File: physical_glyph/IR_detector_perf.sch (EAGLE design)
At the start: 31 parts, among them IC1 7805T, T1 BP103, U1 MCP6004-I/P, U2 LM339PWR

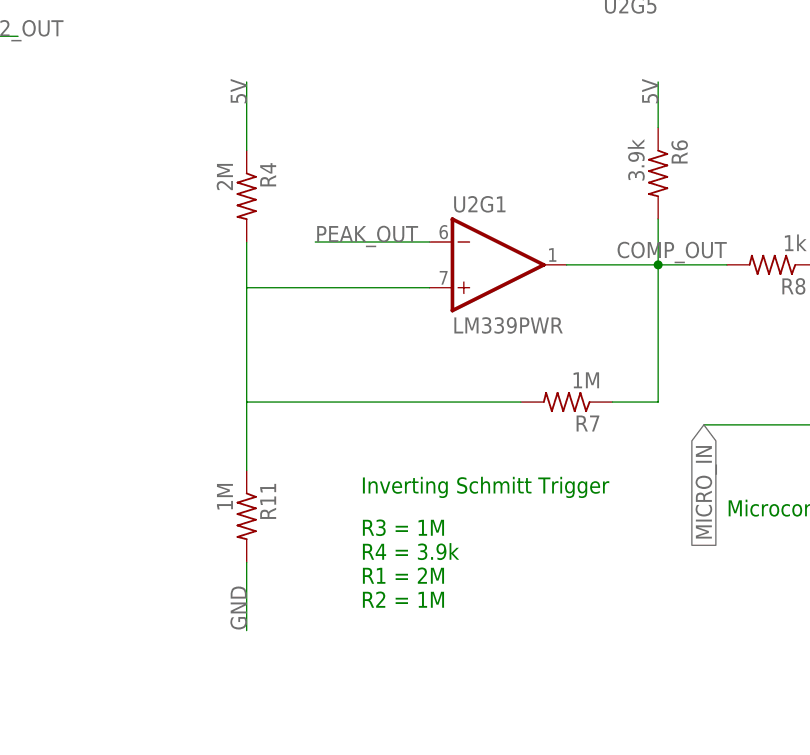
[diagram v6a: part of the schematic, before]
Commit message: Change hystersis upper limit to 2V
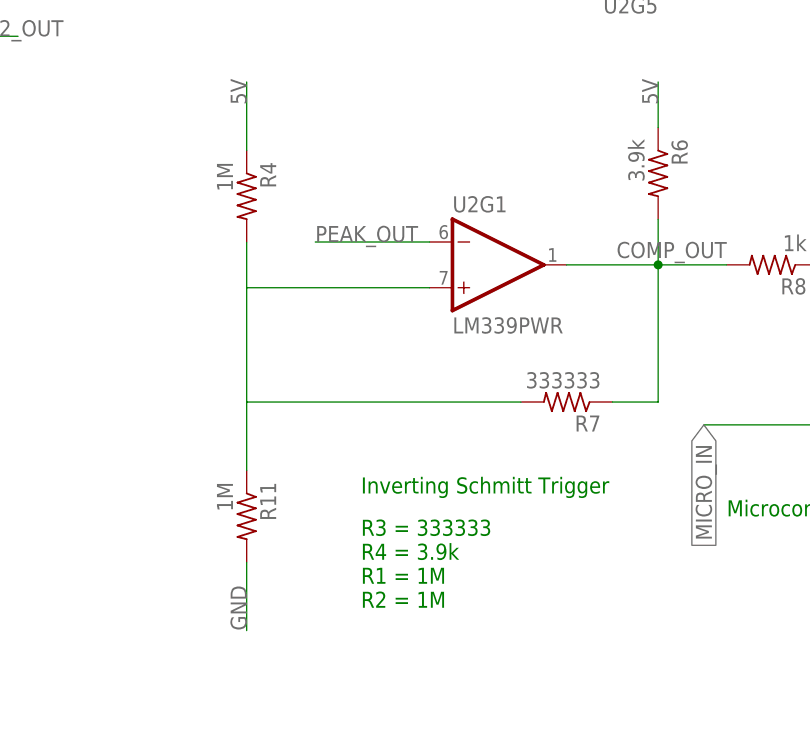
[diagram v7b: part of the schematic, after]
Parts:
- R4: value 2M -> 1M
- R7: value 1M -> 333333
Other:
- note added: "R3 = 333333 R4 = 3.9k R1 = 1M R2 = 1M"
- note removed: "R3 = 1M R4 = 3.9k R1 = 2M R2 = 1M"
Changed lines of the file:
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@@
 <part name="R2" library="rcl" library_urn="urn:adsk.eagle:library:334" deviceset="R-US_" device="0204/2V" package3d_urn="urn:adsk.eagle:package:23495/1" value="1k"/>
 <part name="R3" library="rcl" library_urn="urn:adsk.eagle:library:334" deviceset="R-US_" device="0204/2V" package3d_urn="urn:adsk.eagle:package:23495/1" value="10k"/>
-<part name="R4" library="rcl" library_urn="urn:adsk.eagle:library:334" deviceset="R-US_" device="0204/2V" package3d_urn="urn:adsk.eagle:package:23495/1" value="2M"/>
-<part name="R7" library="rcl" library_urn="urn:adsk.eagle:library:334" deviceset="R-US_" device="0204/2V" package3d_urn="urn:adsk.eagle:package:23495/1" value="1M"/>
+<part name="R4" library="rcl" library_urn="urn:adsk.eagle:library:334" deviceset="R-US_" device="0204/2V" package3d_urn="urn:adsk.eagle:package:23495/1" value="1M"/>
+<part name="R7" library="rcl" library_urn="urn:adsk.eagle:library:334" deviceset="R-US_" device="0204/2V" package3d_urn="urn:adsk.eagle:package:23495/1" value="333333"/>
 <part name="R11" library="rcl" library_urn="urn:adsk.eagle:library:334" deviceset="R-US_" device="0204/2V" package3d_urn="urn:adsk.eagle:package:23495/1" value="1M"/>
 <part name="C3" library="resistor" library_urn="urn:adsk.eagle:library:348" deviceset="C-EU" device="025-024X044" package3d_urn="urn:adsk.eagle:package:26149/1" value="0.1uF"/>
@@
 Amp B: Peak Detector
 Amp C: Split Rail Buffer</text>
-<text x="78.74" y="-27.94" size="1.778" layer="91">R3 = 1M
+<text x="78.74" y="-27.94" size="1.778" layer="91">R3 = 333333
 R4 = 3.9k
-R1 = 2M
+R1 = 1M
 R2 = 1M</text>
 <text x="12.7" y="-58.42" size="1.778" layer="91">RC value = peak detector "leak"</text>

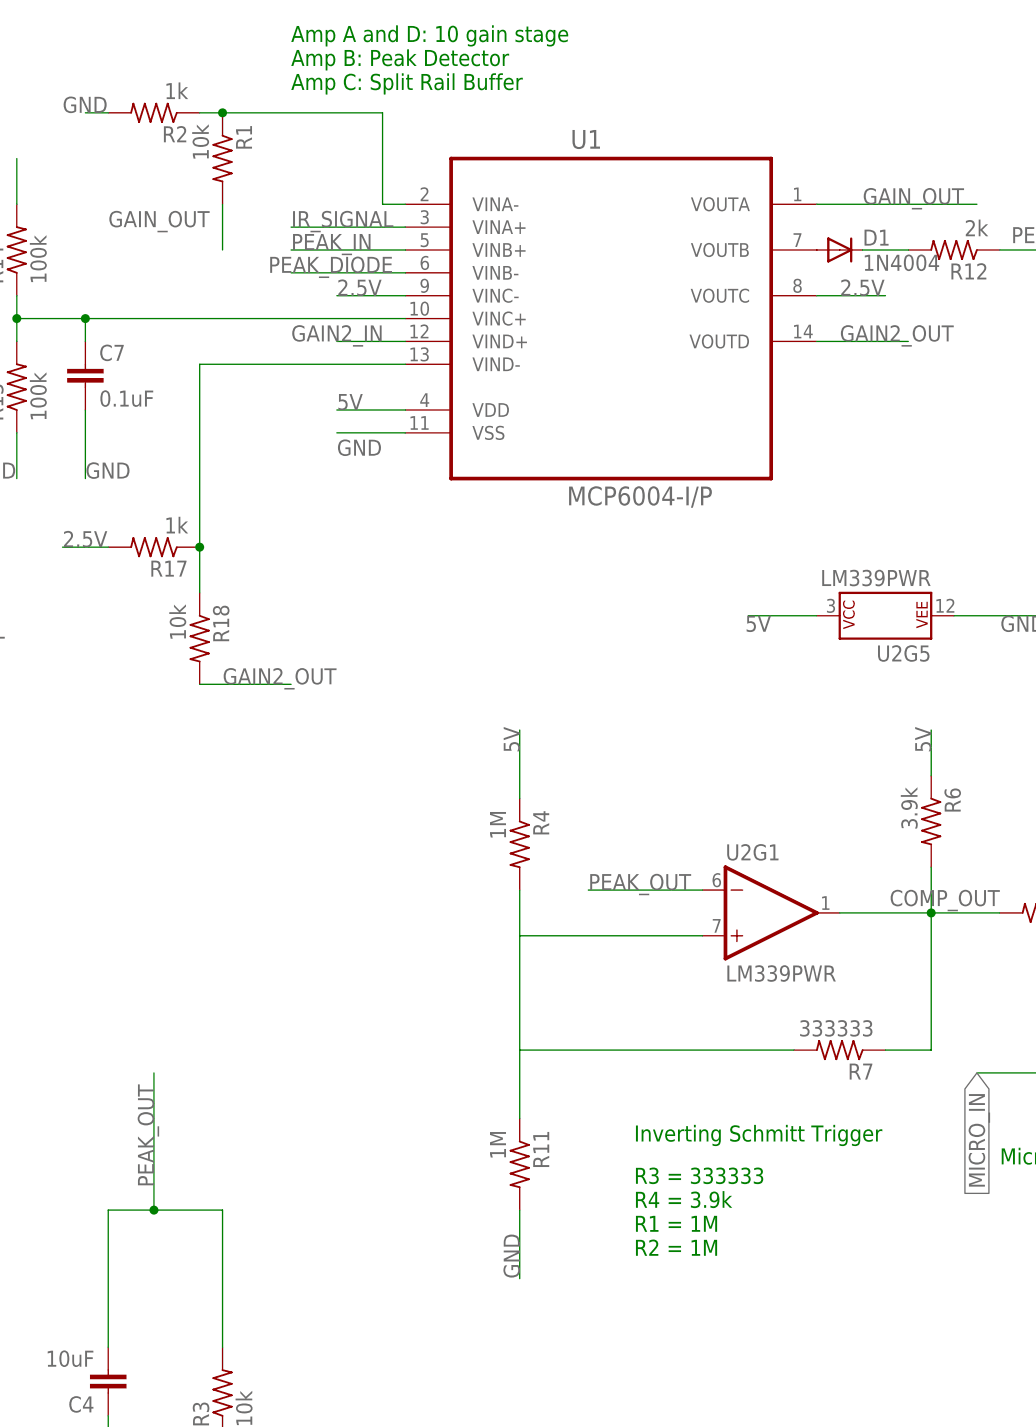
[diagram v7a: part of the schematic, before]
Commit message: Change gain resistors, fix net issue
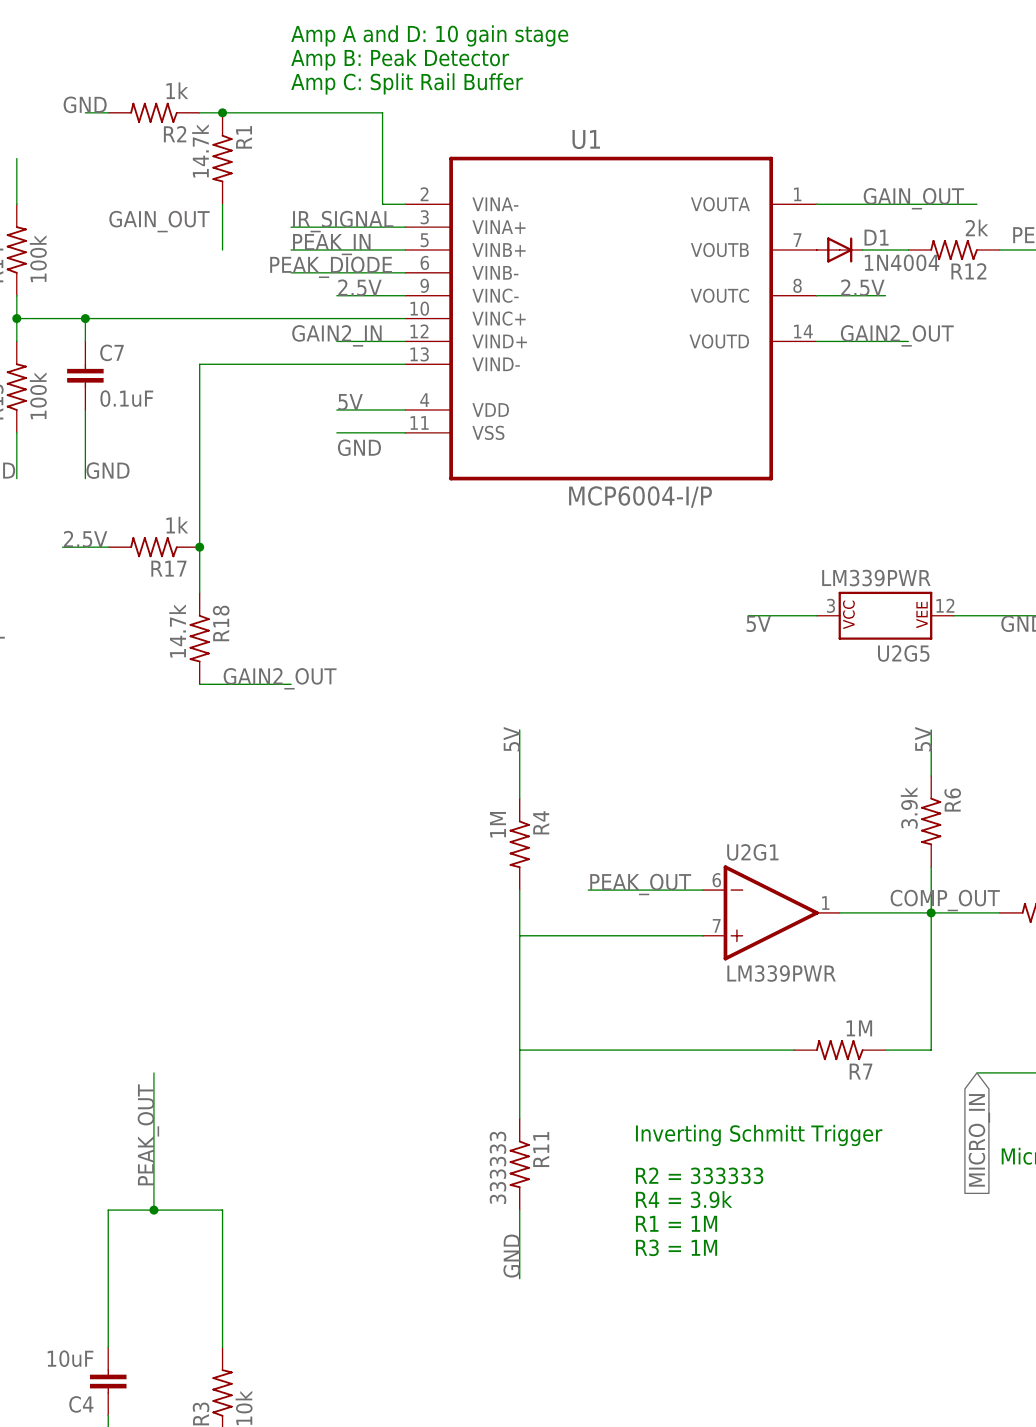
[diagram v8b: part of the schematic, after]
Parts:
- R1, R18: value 10k -> 14.7k
- R11: value 1M -> 333333
- R7: value 333333 -> 1M
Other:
- note added: "R2 = 333333 R4 = 3.9k R1 = 1M R3 = 1M"
- note removed: "R3 = 333333 R4 = 3.9k R1 = 1M R2 = 1M"
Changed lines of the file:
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@@
 <?xml version="1.0" encoding="utf-8"?>
 <!DOCTYPE eagle SYSTEM "eagle.dtd">
-<eagle version="8.6.0">
+<eagle version="9.0.0">
 <drawing>
 <settings>
@@
 <part name="R3" library="rcl" library_urn="urn:adsk.eagle:library:334" deviceset="R-US_" device="0204/2V" package3d_urn="urn:adsk.eagle:package:23495/1" value="10k"/>
 <part name="R4" library="rcl" library_urn="urn:adsk.eagle:library:334" deviceset="R-US_" device="0204/2V" package3d_urn="urn:adsk.eagle:package:23495/1" value="1M"/>
-<part name="R7" library="rcl" library_urn="urn:adsk.eagle:library:334" deviceset="R-US_" device="0204/2V" package3d_urn="urn:adsk.eagle:package:23495/1" value="333333"/>
-<part name="R11" library="rcl" library_urn="urn:adsk.eagle:library:334" deviceset="R-US_" device="0204/2V" package3d_urn="urn:adsk.eagle:package:23495/1" value="1M"/>
+<part name="R7" library="rcl" library_urn="urn:adsk.eagle:library:334" deviceset="R-US_" device="0204/2V" package3d_urn="urn:adsk.eagle:package:23495/1" value="1M"/>
+<part name="R11" library="rcl" library_urn="urn:adsk.eagle:library:334" deviceset="R-US_" device="0204/2V" package3d_urn="urn:adsk.eagle:package:23495/1" value="333333"/>
 <part name="C3" library="resistor" library_urn="urn:adsk.eagle:library:348" deviceset="C-EU" device="025-024X044" package3d_urn="urn:adsk.eagle:package:26149/1" value="0.1uF"/>
 <part name="C4" library="resistor" library_urn="urn:adsk.eagle:library:348" deviceset="C-EU" device="025-024X044" package3d_urn="urn:adsk.eagle:package:26149/1" value="10uF"/>
@@
 <part name="R15" library="rcl" library_urn="urn:adsk.eagle:library:334" deviceset="R-US_" device="0204/2V" package3d_urn="urn:adsk.eagle:package:23495/1" value="100k"/>
 <part name="C7" library="resistor" library_urn="urn:adsk.eagle:library:348" deviceset="C-EU" device="025-024X044" package3d_urn="urn:adsk.eagle:package:26149/1" value="0.1uF"/>
-<part name="R1" library="rcl" library_urn="urn:adsk.eagle:library:334" deviceset="R-US_" device="0204/2V" package3d_urn="urn:adsk.eagle:package:23495/1" value="10k"/>
+<part name="R1" library="rcl" library_urn="urn:adsk.eagle:library:334" deviceset="R-US_" device="0204/2V" package3d_urn="urn:adsk.eagle:package:23495/1" value="14.7k"/>
 <part name="C8" library="resistor" library_urn="urn:adsk.eagle:library:348" deviceset="C-EU" device="025-024X044" package3d_urn="urn:adsk.eagle:package:26149/1" value="0.1uF"/>
 <part name="R16" library="rcl" library_urn="urn:adsk.eagle:library:334" deviceset="R-US_" device="0204/2V" package3d_urn="urn:adsk.eagle:package:23495/1" value="100k"/>
 <part name="R17" library="rcl" library_urn="urn:adsk.eagle:library:334" deviceset="R-US_" device="0204/2V" package3d_urn="urn:adsk.eagle:package:23495/1" value="1k"/>
-<part name="R18" library="rcl" library_urn="urn:adsk.eagle:library:334" deviceset="R-US_" device="0204/2V" package3d_urn="urn:adsk.eagle:package:23495/1" value="10k"/>
+<part name="R18" library="rcl" library_urn="urn:adsk.eagle:library:334" deviceset="R-US_" device="0204/2V" package3d_urn="urn:adsk.eagle:package:23495/1" value="14.7k"/>
 </parts>
 <sheets>
@@
 Amp B: Peak Detector
 Amp C: Split Rail Buffer</text>
-<text x="78.74" y="-27.94" size="1.778" layer="91">R3 = 333333
+<text x="78.74" y="-27.94" size="1.778" layer="91">R2 = 333333
 R4 = 3.9k
 R1 = 1M
-R2 = 1M</text>
+R3 = 1M</text>
 <text x="12.7" y="-58.42" size="1.778" layer="91">RC value = peak detector "leak"</text>
 <text x="78.74" y="-15.24" size="1.778" layer="91">Inverting Schmitt Trigger</text>
